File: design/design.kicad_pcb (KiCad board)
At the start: 2 copper layers, 76.2 x 68.6 mm, 30 parts, among them J1 Conn_01x03_Pin, J2 Conn_01x02_Pin, J3 Conn_01x02_Pin, U1 MC7912, U2 L7812, U3 OPA209AID, U4 TL081, U5 TL081

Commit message: update
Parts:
- moved J3 17.0 mm to (142.2, 111.8)
- moved U5 13.7 mm to (151.1, 108.0), turned to 90 degrees
- moved C7 7.95 mm to (165.1, 91.4), turned to 0 degrees
- moved R10 2.54 mm to (174.0, 99.1)
- moved R8 1.27 mm to (160.0, 94.0)
- moved C6 1.04 mm to (149.9, 88.9)
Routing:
- net Earth: track 76.1 -> 170.8 mm
- net Net-(J3-Pin_1): track 0.00 -> 37.4 mm
- net -12V: track 135.2 -> 172.4 mm
- net +12V: track 53.2 -> 86.8 mm
- net Net-(U5-+): track 0.00 -> 31.3 mm
- net load: track 52.7 -> 67.2 mm
- net Net-(U3-OUT): track 0.93 -> 15.1 mm
- net Net-(R7-Pad1): track 5.08 -> 12.5 mm

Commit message: .
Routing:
- net Earth: track 170.8 -> 118.2 mm
- net Net-(J3-Pin_1): track 37.4 -> 34.5 mm
- net -12V: track 172.4 -> 173.9 mm

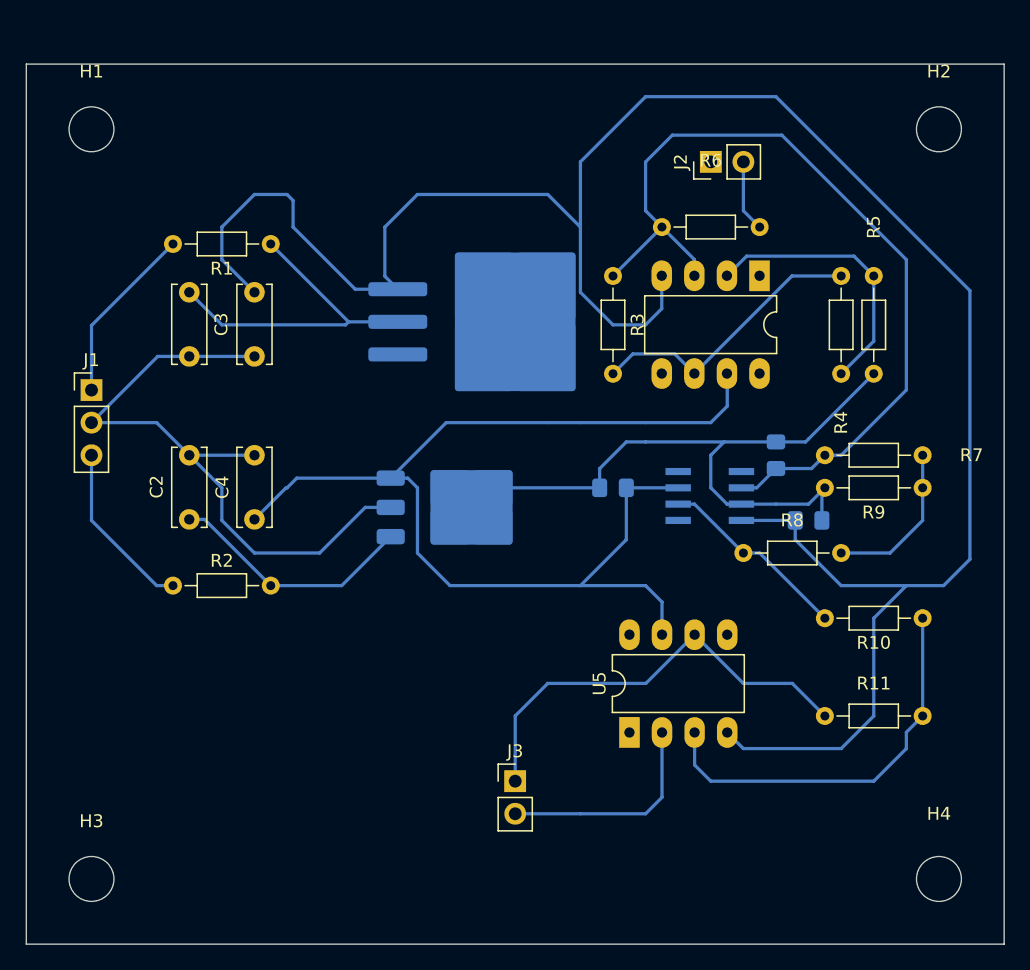
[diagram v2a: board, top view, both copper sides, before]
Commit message: Estan todos los ruteos hechos y DRC verificado. Falta engrosar tracks para mayores 10mils y agregar ground plane
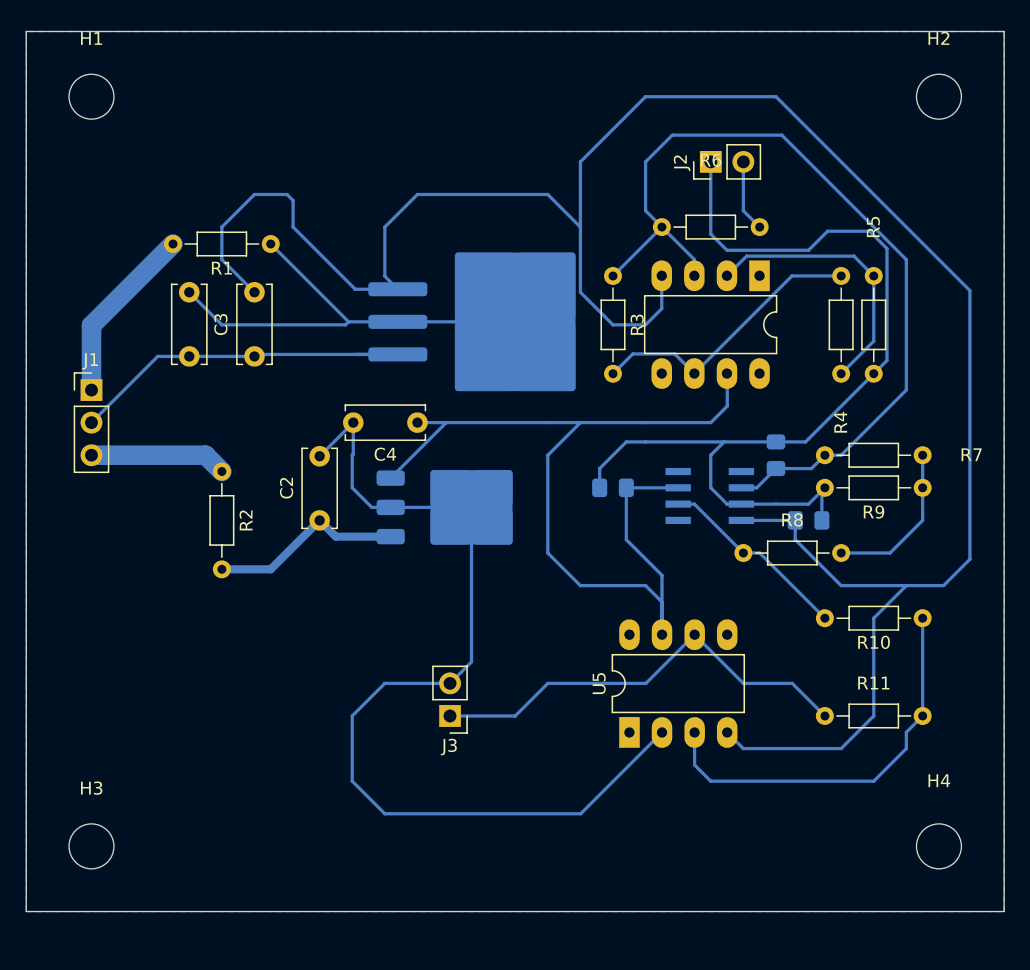
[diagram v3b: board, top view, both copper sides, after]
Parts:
- moved C4 14.8 mm to (134.6, 83.8), turned to 180 degrees
- moved C2 10.2 mm to (127.0, 91.4)
- moved R2 9.67 mm to (119.4, 87.6), turned to -90 degrees
- moved J3 7.18 mm to (137.2, 106.7), turned to 180 degrees
- moved H1 2.54 mm to (109.2, 58.4)
- moved H2 2.54 mm to (175.3, 58.4)
- moved H3 2.54 mm to (109.2, 116.8)
- moved H4 2.54 mm to (175.3, 116.8)
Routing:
- net Earth: track 118.2 -> 177.9 mm
- net +12V: track 86.8 -> 74.2 mm
- net Net-(U1-VI): track 26.0 -> 35.1 mm
- net Net-(U2-IN): track 19.4 -> 15.3 mm
- net Net-(J1-Pin_3): track 13.5 -> 10.7 mm
- added copper zone on B.Cu, net Earth
